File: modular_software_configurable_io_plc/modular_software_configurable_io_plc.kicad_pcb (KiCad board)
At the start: 4 copper layers, 105 x 107 mm, 36 parts, among them J1 FW-14-03-G-D-085-155, J10 CLP-108-02-G-D-BE, J11 CLP-102-02-G-D-BE, J12 CLP-102-02-G-D-BE, J13 CLP-102-02-G-D-BE, J14 CLP-108-02-G-D-BE, J15 FW-14-03-G-D-085-155, J16 FW-02-03-G-D-085-155, J17 FW-02-03-G-D-085-155, J18 FW-02-03-G-D-085-155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

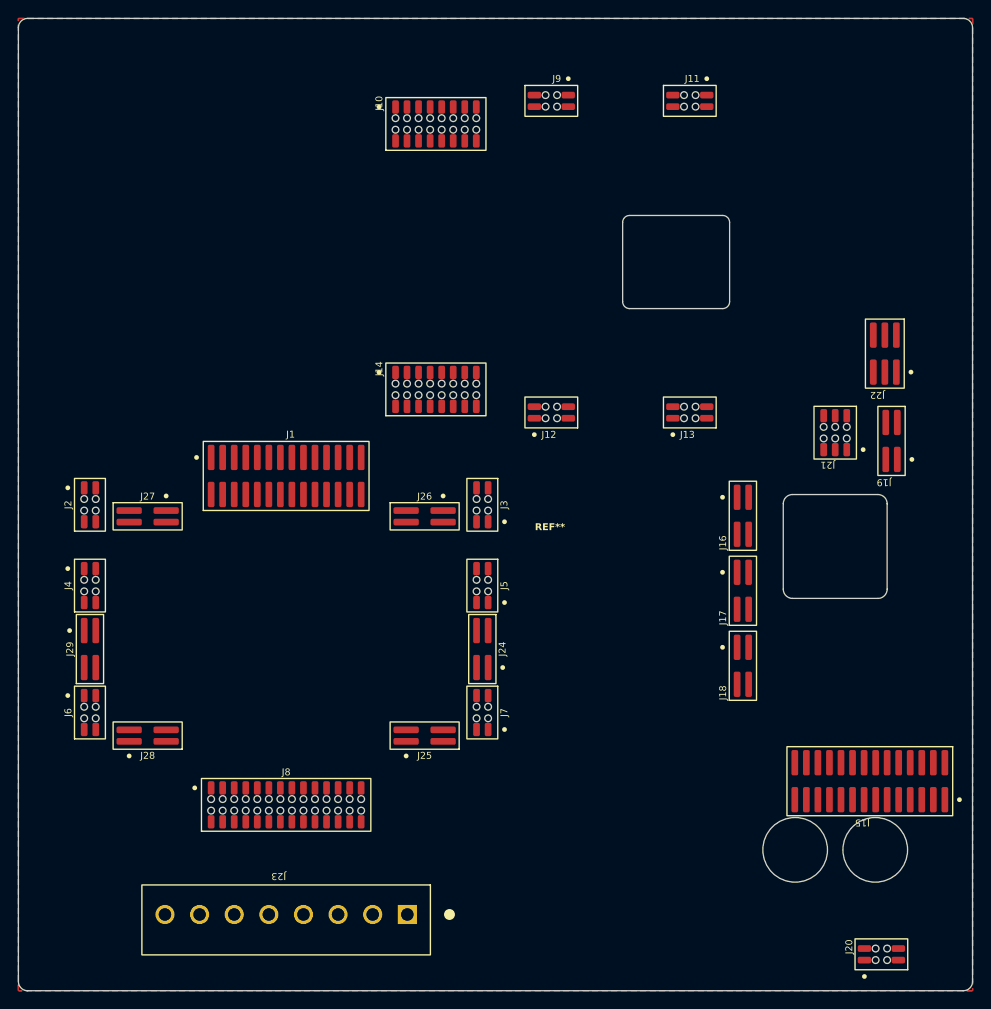
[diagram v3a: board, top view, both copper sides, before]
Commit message: Update KiCAD Symbol Generator submodule to latest commit
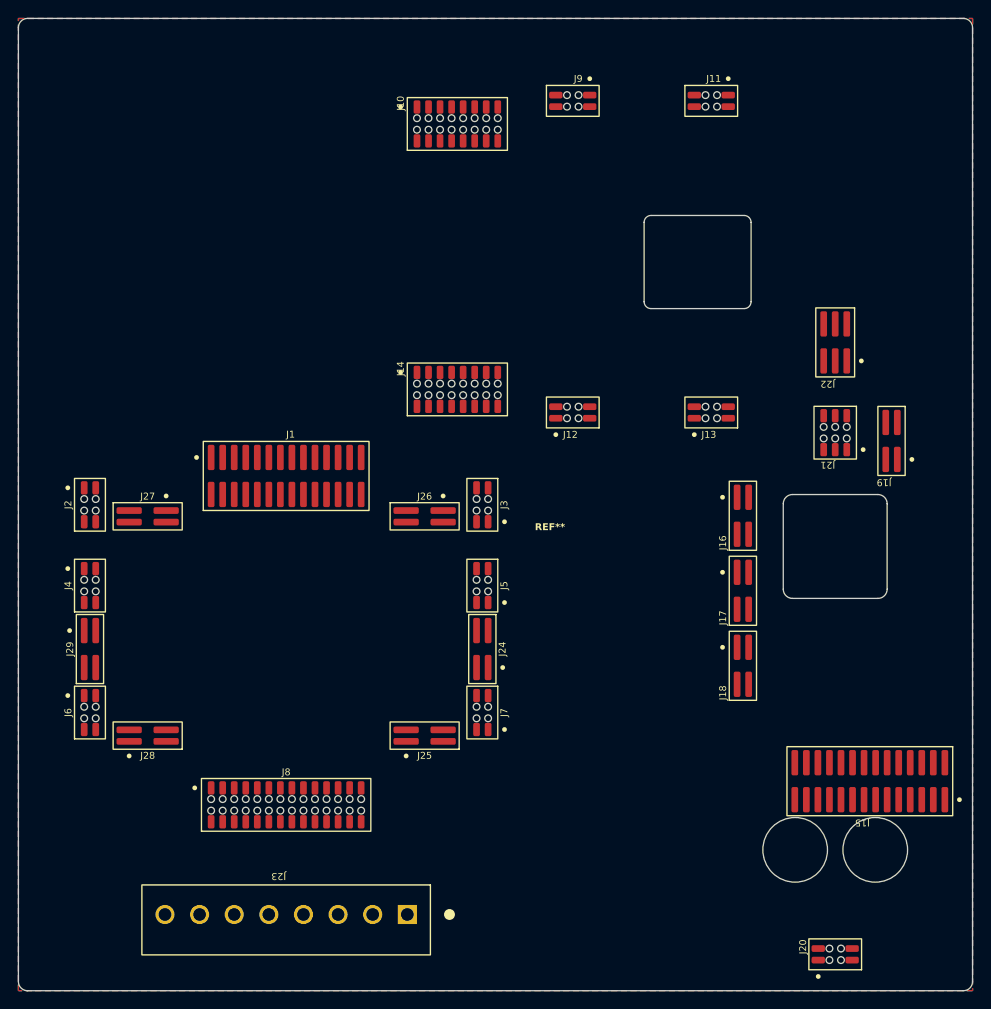
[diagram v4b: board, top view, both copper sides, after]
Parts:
- moved J22 5.60 mm to (215.1, 75.9)
- moved J20 5.08 mm to (215.1, 143.2)
- moved MOD6 4.18 mm to (217.6, 60.6)
- moved J10 2.36 mm to (173.5, 51.8)
- moved J11 2.36 mm to (201.5, 49.3)
- moved J12 2.36 mm to (186.2, 83.6)
- moved J13 2.36 mm to (201.5, 83.6)
- moved J14 2.36 mm to (173.5, 81.0)
- moved J9 2.36 mm to (186.2, 49.3)
- moved MOD3 2.36 mm to (191.3, 66.4)
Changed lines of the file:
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@@
 		)
 		(property "Footprint" "connector_footprints:FW-02-03-G-D-085-155"
-			(at 0 0 360)
+			(at 0 0 0)
 			(layer "F.Fab")
 			(hide yes)
@@
 		)
 		(property "Datasheet" "https://suddendocs.samtec.com/catalog_english/fw_sm.pdf?_gl=1*1xtxv9c*_gcl_au*MTM0MTYyNTQ5MS4xNzM2MDk5MTUz*_ga*MTYxNDYyMTQ0Mi4xNzM2MDk5MTUz*_ga_3KFNZC07WW*MTczODE2NTI0NS4zMi4xLjE3MzgxNjU1NjMuNjAuMC4w"
-			(at 0 0 360)
+			(at 0 0 0)
 			(layer "F.Fab")
 			(hide yes)
@@
 		)
 		(property "Description" "Samtec FW-xx-03-G-D-085-155 series,  2 positions connector,  1.27 mm pitch,  Black,  Vertical mounting,  5.2 A,  300 V,  Surface Mount,  Gold plated"
-			(at 0 0 360)
+			(at 0 0 0)
 			(layer "F.Fab")
 			(hide yes)
@@
 		)
 		(property "Footprint" "connector_footprints:FW-02-03-G-D-085-155"
-			(at 0 0 360)
+			(at 0 0 0)
 			(layer "F.Fab")
 			(hide yes)
@@
 		)
 		(property "Datasheet" "https://suddendocs.samtec.com/catalog_english/fw_sm.pdf?_gl=1*1xtxv9c*_gcl_au*MTM0MTYyNTQ5MS4xNzM2MDk5MTUz*_ga*MTYxNDYyMTQ0Mi4xNzM2MDk5MTUz*_ga_3KFNZC07WW*MTczODE2NTI0NS4zMi4xLjE3MzgxNjU1NjMuNjAuMC4w"
-			(at 0 0 360)
+			(at 0 0 0)
 			(layer "F.Fab")
 			(hide yes)
@@
 		)
 		(property "Description" "Samtec FW-xx-03-G-D-085-155 series,  2 positions connector,  1.27 mm pitch,  Black,  Vertical mounting,  5.2 A,  300 V,  Surface Mount,  Gold plated"
-			(at 0 0 360)
+			(at 0 0 0)
 			(layer "F.Fab")
 			(hide yes)
@@
 	(footprint "modules_footprints:minimal_adp1032"
 		(layer "F.Cu")
-		(at 188.92012 66.421)
+		(at 191.28232 66.421)
 		(property "Reference" "MOD3"
 			(at 0.00508 0 0)
@@
 	(footprint "connector_footprints:FW-03-03-G-D-085-155"
 		(layer "F.Cu")
-		(at 220.56852 77.089 180)
+		(at 215.10752 75.8571 180)
 		(property "Reference" "J22"
 			(at 0 -4.572 180)
@@
 	(footprint "connector_footprints:CLP-102-02-G-D-BE"
 		(layer "F.Cu")
-		(at 199.10552 83.566 90)
+		(at 201.46772 83.566 90)
 		(property "Reference" "J13"
 			(at -2.44 -1.085 0)
@@
 		)
 		(property "Footprint" "connector_footprints:FW-02-03-G-D-085-155"
-			(at 0 0 360)
+			(at 0 0 0)
 			(layer "F.Fab")
 			(hide yes)
@@
 		)
 		(property "Datasheet" "https://suddendocs.samtec.com/catalog_english/fw_sm.pdf?_gl=1*1xtxv9c*_gcl_au*MTM0MTYyNTQ5MS4xNzM2MDk5MTUz*_ga*MTYxNDYyMTQ0Mi4xNzM2MDk5MTUz*_ga_3KFNZC07WW*MTczODE2NTI0NS4zMi4xLjE3MzgxNjU1NjMuNjAuMC4w"
-			(at 0 0 360)
+			(at 0 0 0)
 			(layer "F.Fab")
 			(hide yes)
@@
 		)
 		(property "Description" "Samtec FW-xx-03-G-D-085-155 series,  2 positions connector,  1.27 mm pitch,  Black,  Vertical mounting,  5.2 A,  300 V,  Surface Mount,  Gold plated"
-			(at 0 0 360)
+			(at 0 0 0)
 			(layer "F.Fab")
 			(hide yes)
@@
 	(footprint "connector_footprints:CLP-102-02-G-D-BE"
 		(layer "F.Cu")
-		(at 199.10552 49.276 -90)
+		(at 201.46772 49.276 -90)
 		(property "Reference" "J11"
 			(at -2.44 -1.085 0)
@@
 	(footprint "connector_footprints:CLP-108-02-G-D-BE"
 		(layer "F.Cu")
-		(at 171.16552 51.816)
+		(at 173.52772 51.816)
 		(property "Reference" "J10"
 			(at -6.25 -1.455 90)
@@
 	(footprint "connector_footprints:CLP-108-02-G-D-BE"
 		(layer "F.Cu")
-		(at 171.16552 81.026)
+		(at 173.52772 81.026)
 		(property "Reference" "J14"
 			(at -6.25 -1.455 90)
@@
 	(footprint "connector_footprints:CLP-102-02-G-D-BE"
 		(layer "F.Cu")
-		(at 183.86552 83.566 90)
+		(at 186.22772 83.566 90)
 		(property "Reference" "J12"
 			(at -2.44 -1.085 0)
@@
 	(footprint "connector_footprints:CLP-102-02-G-D-BE"
 		(layer "F.Cu")
-		(at 183.86552 49.276 -90)
+		(at 186.22772 49.276 -90)
 		(property "Reference" "J9"
 			(at -2.44 -1.085 0)
@@
 	(footprint "connector_footprints:CLP-102-02-G-D-BE"
 		(layer "F.Cu")
-		(at 220.18752 143.1925 90)
+		(at 215.10752 143.1925 90)
 		(property "Reference" "J20"
 			(at 0 -3.556 90)
@@
 	(footprint "modules_footprints:minimal_spoe_hybrid"
 		(layer "F.Cu")
-		(at 220.56852 57.658 -90)
+		(at 217.64752 60.6425 -90)
 		(property "Reference" "MOD6"
 			(at 0.00254 -0.5 -90)
@@
 		(sheetfile "modular_software_configurable_io_plc.kicad_sch")
 		(fp_line
-			(start 15.24 9.144)
-			(end -15.24 9.144)
+			(start 10.795 9.144)
+			(end -18.415 9.144)
 			(stroke
 				(width 0.05)
@@
 		)
 		(fp_line
-			(start -15.875 8.509)
-			(end -15.875 -8.509)
+			(start -19.05 8.509)
+			(end -19.05 -8.509)
 			(stroke
 				(width 0.05)
@@
 		)
 		(fp_line
-			(start 22.86 3.81)
-			(end 17.78 3.81)
+			(start 18.415 6.35)
+			(end 13.335 6.35)
 			(stroke
 				(width 0.05)
@@
 		)
 		(fp_line
-			(start 15.875 3.175)
-			(end 15.875 8.509)
+			(start 11.43 5.715)
+			(end 11.43 8.509)
 			(stroke
 				(width 0.05)
@@
 		)
 		(fp_line
-			(start 15.875 -3.175)
-			(end 15.875 -8.509)
+			(start 11.43 -0.635)
+			(end 11.43 -8.509)
 			(stroke
 				(width 0.05)
@@
 		)
 		(fp_line
-			(start 23.495 -3.175)
-			(end 23.495 3.175)
+			(start 19.05 -0.635)
+			(end 19.05 5.715)
 			(stroke
 				(width 0.05)
@@
 		)
 		(fp_line
-			(start 17.78 -3.81)
-			(end 22.86 -3.81)
+			(start 13.335 -1.27)
+			(end 18.415 -1.27)
 			(stroke
 				(width 0.05)
@@
 		)
 		(fp_line
-			(start -15.24 -9.144)
-			(end 15.24 -9.144)
+			(start -18.415 -9.144)
+			(end 10.795 -9.144)
 			(stroke
 				(width 0.05)
@@
 		)
 		(fp_arc
-			(start -15.24 9.144)
-			(mid -15.689013 8.958013)
-			(end -15.875 8.509)
+			(start -18.415 9.144)
+			(mid -18.864013 8.958013)
+			(end -19.05 8.509)
 			(stroke
 				(width 0.05)
@@
 		)
 		(fp_arc
-			(start 15.875 8.509)
-			(mid 15.689013 8.958013)
-			(end 15.24 9.144)
+			(start 11.43 8.509)
+			(mid 11.244013 8.958013)
+			(end 10.795 9.144)
 			(stroke
 				(width 0.05)
@@
 		)
 		(fp_arc
-			(start 17.78 3.81)
-			(mid 17.330987 3.624013)
-			(end 17.145 3.175)
+			(start 13.335 6.35)
+			(mid 12.885987 6.164013)
+			(end 12.7 5.715)
 			(stroke
 				(width 0.05)
@@
 		)
 		(fp_arc
-			(start 15.875 3.175)
-			(mid 16.060987 2.725987)
-			(end 16.51 2.54)
+			(start 11.43 5.715)
+			(mid 11.615987 5.265987)
+			(end 12.065 5.08)
 			(stroke
 				(width 0.05)
@@
 		)
 		(fp_arc
-			(start 23.495 3.175)
-			(mid 23.309013 3.624013)
-			(end 22.86 3.81)
+			(start 19.05 5.715)
+			(mid 18.864013 6.164013)
+			(end 18.415 6.35)
 			(stroke
 				(width 0.05)
@@
 		)
 		(fp_arc
-			(start 16.51 2.54)
-			(mid 16.959013 2.725987)
-			(end 17.145 3.175)
+			(start 12.065 5.08)
+			(mid 12.514013 5.265987)
+			(end 12.7 5.715)
 			(stroke
 				(width 0.05)
@@
 		)
 		(fp_arc
-			(start 16.51 -2.54)
-			(mid 16.060987 -2.725987)
-			(end 15.875 -3.175)
+			(start 12.065 0)
+			(mid 11.615987 -0.185987)
+			(end 11.43 -0.635)
 			(stroke
 				(width 0.05)
@@
 		)
 		(fp_arc
-			(start 17.145 -3.175)
-			(mid 16.959013 -2.725987)
-			(end 16.51 -2.54)
+			(start 12.7 -0.635)
+			(mid 12.514013 -0.185987)
+			(end 12.065 0)
 			(stroke
 				(width 0.05)
@@
 		)
 		(fp_arc
-			(start 17.145 -3.175)
-			(mid 17.330987 -3.624013)
-			(end 17.78 -3.81)
+			(start 12.7 -0.635)
+			(mid 12.885987 -1.084013)
+			(end 13.335 -1.27)
 			(stroke
 				(width 0.05)
@@
 		)
 		(fp_arc
-			(start 22.86 -3.81)
-			(mid 23.309013 -3.624013)
-			(end 23.495 -3.175)
+			(start 18.415 -1.27)
+			(mid 18.864013 -1.084013)
+			(end 19.05 -0.635)
 			(stroke
 				(width 0.05)
@@
 		)
 		(fp_arc
-			(start -15.875 -8.509)
-			(mid -15.689013 -8.958013)
-			(end -15.24 -9.144)
+			(start -19.05 -8.509)
+			(mid -18.864013 -8.958013)
+			(end -18.415 -9.144)
 			(stroke
 				(width 0.05)
@@
 		)
 		(fp_arc
-			(start 15.24 -9.144)
-			(mid 15.689013 -8.958013)
-			(end 15.875 -8.509)
+			(start 10.795 -9.144)
+			(mid 11.244013 -8.958013)
+			(end 11.43 -8.509)
 			(stroke
 				(width 0.05)
@@
 		)
 		(fp_circle
-			(center 19.431 0)
-			(end 19.939 0)
+			(center 15.2146 2.54)
+			(end 15.7226 2.54)
 			(stroke
 				(width 0.0254)
@@
 		(model "${KIPRJMOD}/KiCAD_Symbol_Generator/3D_models/minimal_spoe_hybrid.wrl"
 			(offset
-				(xyz 3.81 0 3.048)
+				(xyz 0 0 3.048)
 			)
 			(scale
@@
 		)
 		(property "Footprint" "connector_footprints:CLP-103-02-G-D-BE"
-			(at 0 0 360)
+			(at 0 0 0)
 			(layer "F.Fab")
 			(hide yes)
@@
 		)
 		(property "Datasheet" "https://suddendocs.samtec.com/catalog_english/clp_sm.pdf?_gl=1*1y4jlr9*_gcl_au*MTM0MTYyNTQ5MS4xNzM2MDk5MTUz*_ga*MTYxNDYyMTQ0Mi4xNzM2MDk5MTUz*_ga_3KFNZC07WW*MTczNjY4MDQ4OS4xNS4xLjE3MzY2ODEzNzcuNjAuMC4w"
-			(at 0 0 360)
+			(at 0 0 0)
 			(layer "F.Fab")
 			(hide yes)
@@
 		)
 		(property "Description" "Samtec CLP-1xx-02-G-D-BE series,  3 positions connector,  1.27 mm pitch,  Black,  Vertical mounting,  5.2 A,  300 V,  Surface Mount,  Tin plated"
-			(at 0 0 360)
+			(at 0 0 0)
 			(layer "F.Fab")
 			(hide yes)
@@
 		)
 	)
-	(group ""
-		(members "022c256d-39bb-4b86-a1bc-72c6725ae5ab" "07ed78f3-48b8-4069-8ec7-88c6fd1a98cc"
-			"09246060-0510-4d63-be57-8bc848da2e3a" "0e6ef412-b2df-4bbc-97c0-2d32c44fa772"
-			"1424bcac-345d-4ebb-ae69-be5f5f8ff310" "1a32b8f1-ff7a-40c0-ab80-8e8b4982d54b"
-			"1ee81221-5b3b-4fde-97a6-42b7e5b384d4" "21039c19-004b-4ab5-9493-0958c05971ce"
-			"2249f4b5-ebdd-456c-a73b-9486adf6e9c6" "2e91a8eb-df8b-4e4e-a329-74d5b9e72f31"
-			"377ec453-f44b-4cfe-aa81-d79f3d532bd7" "43a26977-6998-4bf7-b493-3e95c81624f4"
-			"92dc65a3-65bc-4951-b2bc-bef1434724ac" "9f8d78b4-0d99-4a3d-a23e-e1febdca37f0"
-			"a8c72e5e-349c-4214-8a1f-9385cabd641d" "a9ec3c60-6a17-4974-acf3-54a129d1d1e7"
-			"ac047768-4b6b-4188-beee-7317fcd88fa4" "b0c8a0e1-9416-4d9b-9b27-ad65ecf4d93f"
-			"b7ca015d-fc7e-4745-936b-2dc41521adf0" "bd467b9a-475c-4471-8e4d-5fcffd85298a"
-			"c3aee30c-4cfc-41a4-ad30-2619433bc350" "c5cff21f-3466-4d84-8206-ea6c2be84020"
-			"c764a7cd-6dba-494f-9563-a24723499a3f" "c76f0412-1825-4a85-8853-ea74a83259a9"
-			"d6d9fbf5-ea0b-4ee5-b87b-5183bc7f64d2" "dfc409ac-0486-4822-89cc-53f9f216e5e3"
-			"e4376b9c-7d51-4006-bdf2-bc8cf75d68d4" "e9d62d4c-1c11-46b1-9ac3-803411f66ebf"
-			"f26c57bd-4589-4c6c-a305-ec3b2af2776a"
-		)
-	)

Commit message: Backup
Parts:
- removed REF**: 2907525, mechanical_parts:U_2907525
- J19: footprint connector_footprints:FW-02-03-G-D-085-155 -> connector_footprints:FW-03-03-G-D-085-155
- moved MOD4 5.13 mm to (215.9, 104.1)
- moved J19 2.24 mm to (220.8, 84.5), turned to 0 degrees
- moved J15 0.65 mm to (219.0, 123.5)
- moved J16 0.65 mm to (205.1, 94.3)
- moved J17 0.65 mm to (205.1, 102.6)
- moved J18 0.65 mm to (205.1, 110.8)
- turned J21 to 0 degrees
